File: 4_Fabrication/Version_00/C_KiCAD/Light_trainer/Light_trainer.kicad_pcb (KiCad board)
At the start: 2 copper layers, 70 parts, among them J1 USB_B_Micro, J2 Conn_01x02_Batterie, Q1 DMG3414U, Q2 S8050, Q3 S8050, SW1 SW_Push, SW2 SW_Push, SW3 SW_Push, SW4 SW_Push, SW5 SW_Push, SW6 SW_DIP_x04, SW7 SW_Push, U1 MCP73831-2-OT, U2 ESP32-WROOM-32, U3 LTC3525-5, U4 AP2112K-3.3, U5 CP2104

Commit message: modif kicad
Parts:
- removed Q1: DMG3414U, Package_TO_SOT_SMD:SOT-23
- removed R7: 100k, Resistor_SMD:R_0805_2012Metric
- added J3: Conn_01x09_Female, Connector_PinHeader_1.00mm:PinHeader_1x09_P1.00mm_Vertical, B.Cu at (199.4, 96.5)
- added J4: Conn_01x09_Female, Connector_PinHeader_1.00mm:PinHeader_1x09_P1.00mm_Vertical, F.Cu at (223.5, 96.5)
- added L1: 10uH, Inductor_SMD:L_Wuerth_WE_PMI, F.Cu at (170.2, 111.8)
- added S1: SW_DP3T, Button_Switch_THT:SW_DP3T, F.Cu at (259.1, 102.9)
- C14, C15, R12, R9: moved to B.Cu
- C9: value 10uF -> 1uF
- moved D16 108.1 mm to (172.7, 100.3)
- moved C15 106.4 mm to (240.0, 100.3), turned to 270 degrees
- moved C14 100.8 mm to (236.2, 100.3)
- moved D12 100.0 mm to (227.3, 100.3), turned to 90 degrees
- moved D9 99.9 mm to (238.8, 100.3), turned to 90 degrees
- moved D11 99.7 mm to (231.1, 100.3), turned to 90 degrees
- moved D10 99.6 mm to (234.9, 100.3), turned to 90 degrees
- moved R12 93.4 mm to (232.4, 100.3), turned to 270 degrees
- moved R9 91.0 mm to (228.6, 100.3), turned to 270 degrees
- moved D15 88.3 mm to (148.6, 76.2)
- moved R11 83.3 mm to (194.3, 115.6), turned to 0 degrees
- moved D6 80.9 mm to (207.0, 100.3)
- moved D5 80.8 mm to (196.8, 76.2), turned to 0 degrees
- moved R14 80.1 mm to (154.7, 85.9)
- moved R13 80.1 mm to (157.2, 85.9)
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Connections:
- D4 pad 2: VBUS -> batt_on
- R9 pad 1: (no net) -> Net-(R9-Pad1)
- U2 pad 23: (no net) -> info_batt
- U3 pad 6: (no net) -> Net-(L1-Pad1)

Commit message: modif kicad
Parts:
- added J5: Conn_01x02_Batterie, Connector_Wire:SolderWire-0.1sqmm_1x02_P3.6mm_D0.4mm_OD1mm, F.Cu at (181.6, 124.5)
- moved TP3 74.0 mm to (186.7, 77.5)
- moved TP1 71.1 mm to (186.7, 82.5), turned to 0 degrees
- moved TP2 68.6 mm to (186.7, 87.6), turned to 90 degrees
- moved TP5 46.7 mm to (166.4, 100.3)
- moved J2 26.5 mm to (148.6, 106.7)
- moved R16 7.89 mm to (157.5, 86.4)
- moved R13 7.38 mm to (149.9, 86.4)
- moved R15 2.84 mm to (154.9, 86.4)
- moved R14 2.34 mm to (152.4, 86.4)
- moved C12 1.27 mm to (176.5, 111.8)
- moved TP4 0.57 mm to (186.7, 72.4)
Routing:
- net GND: track 0.00 -> 412.6 mm, vias 0 -> 9
- net +3V3: track 0.00 -> 218.3 mm, vias 0 -> 8
- net +5V: track 0.00 -> 209.6 mm, vias 0 -> 6
- net batt_on: track 0.00 -> 108.4 mm, vias 0 -> 1
- net switch: track 0.00 -> 101.7 mm, vias 0 -> 1
- net +BATT: track 0.00 -> 94.3 mm, vias 0 -> 1
- net EN: track 0.00 -> 69.8 mm, vias 0 -> 2
- net LED_B_3: track 0.00 -> 64.1 mm, vias 0 -> 2
- net VBUS: track 0.00 -> 57.1 mm, vias 0 -> 2
- net D+: track 0.00 -> 45.2 mm, vias 0 -> 2
- net Net-(D15-Pad4): track 0.00 -> 41.9 mm, vias 0 -> 2
- net Net-(D14-Pad4): track 0.00 -> 40.8 mm, vias 0 -> 2
- net stat: track 0.00 -> 39.8 mm, vias 0 -> 2
- net S1: track 0.00 -> 38.7 mm, vias 0 -> 2
- net D-: track 0.00 -> 37.9 mm, vias 0 -> 3
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
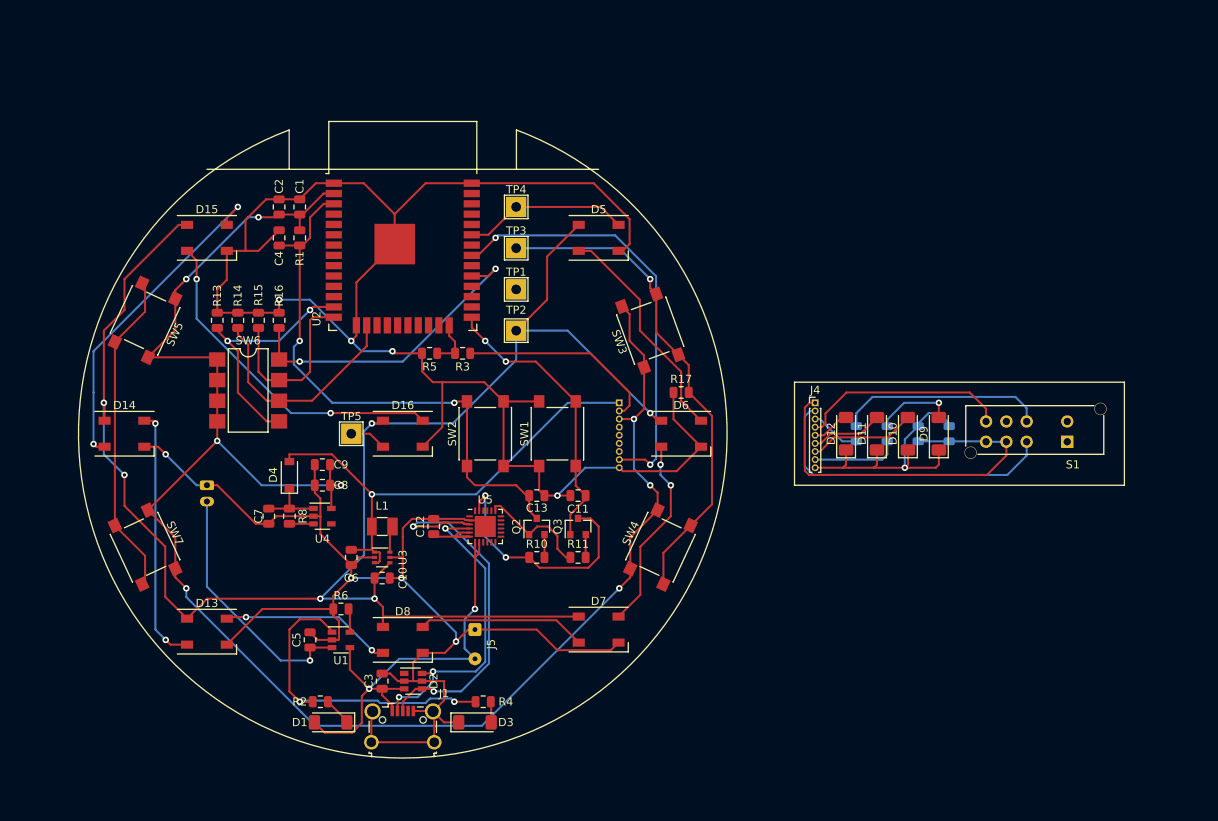
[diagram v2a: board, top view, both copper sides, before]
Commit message: add code
I maybe want to work with pi pico and NRF24l01.
But I have to abandoned my idea of the site web.
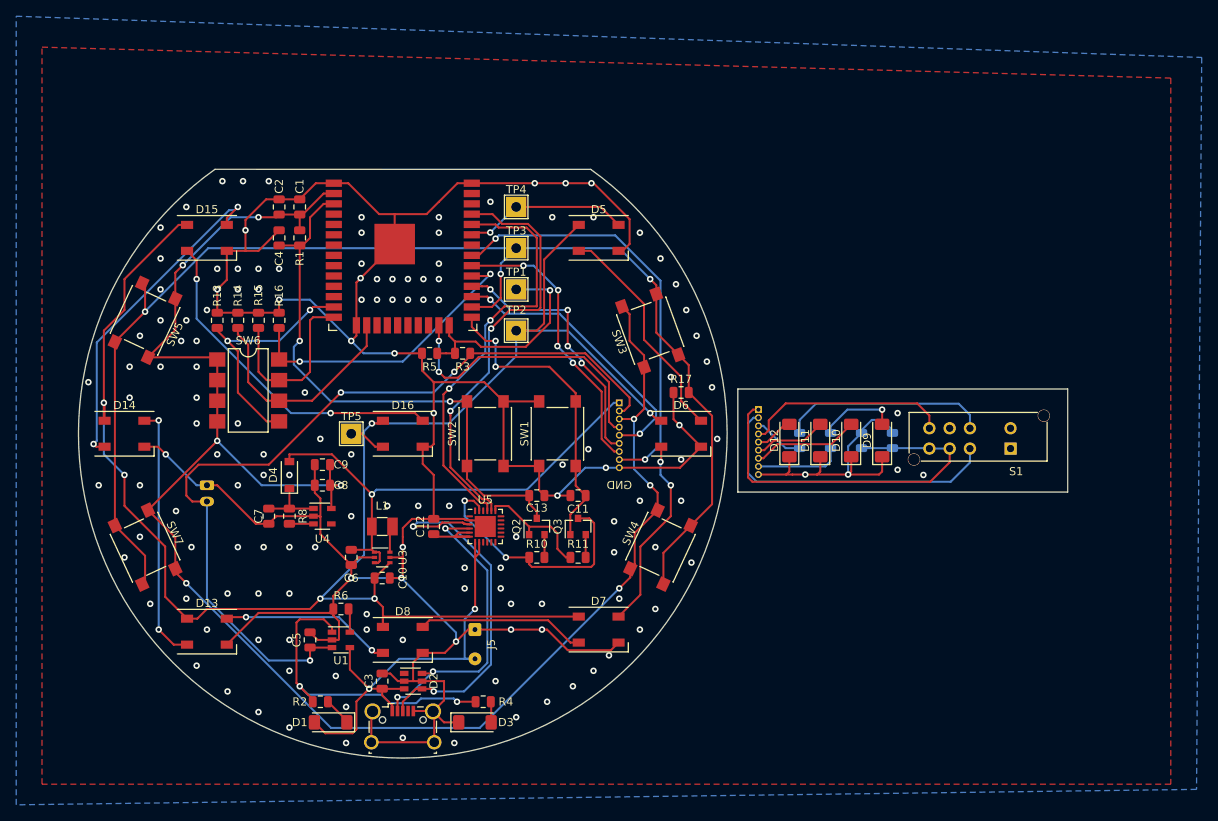
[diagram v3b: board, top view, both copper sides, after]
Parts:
- J4: moved to B.Cu
- moved C15 7.04 mm to (233.0, 101.2)
- moved D12 7.04 mm to (220.3, 101.2)
- moved J4 7.04 mm to (216.5, 97.4), turned to 180 degrees
- moved C14 7.04 mm to (229.2, 101.2)
- moved D10 7.04 mm to (228.0, 101.2)
- moved D11 7.04 mm to (224.2, 101.2)
- moved D9 7.04 mm to (231.8, 101.2)
- moved R12 7.04 mm to (225.4, 101.2)
- moved R9 7.04 mm to (221.6, 101.2)
- moved S1 7.04 mm to (252.1, 103.7)
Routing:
- net switch: track 101.7 -> 161.7 mm, vias 1 -> 3
- net RXD: track 0.00 -> 52.5 mm, vias 0 -> 2
- net TXD: track 0.00 -> 52.0 mm, vias 0 -> 2
- net +BATT: track 94.3 -> 141.3 mm, vias 1 -> 3
- net LED_B_2: track 13.2 -> 48.5 mm, vias 0 -> 4
- net info_batt: track 25.9 -> 61.3 mm, vias 0 -> 2
- net LED_B_0: track 4.72 -> 39.6 mm, vias 0 -> 2
- net LED_B_1: track 8.94 -> 41.6 mm, vias 0 -> 4
- net Net-(R3-Pad2): track 5.93 -> 28.1 mm, vias 0 -> 1
- net GND: track 412.6 -> 421.8 mm, vias 9 -> 148
- net IO0: track 35.5 -> 38.0 mm
- net S1: track 38.7 -> 36.9 mm
- net +5V: track 209.6 -> 210.8 mm
- net VBUS: track 57.1 -> 58.0 mm
- net DTR: track 30.1 -> 31.0 mm
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- added copper zone on B.Cu, net GND
- added copper zone on F.Cu, net GND
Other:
- board outline added: 121.9 x 72.5 mm
- board text added: "GND"
- board text added: "Light Trainer V0 Copyright 2020/2021 Robin Forestier"

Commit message: add datasheet
Restart the project
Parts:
- removed C14, C5, C7, C8: 10uF, Capacitor_SMD:C_0805_2012Metric
- removed C15: 0,1uF, Capacitor_SMD:C_0805_2012Metric
- removed C9: 1uF, Capacitor_SMD:C_0805_2012Metric
- removed D1, D9: LED_R, LED_SMD:LED_1806_4516Metric
- removed D10, D11, D12, D3: LED_G, LED_SMD:LED_1806_4516Metric
- removed D4: MBR0540, Diode_SMD:D_SOD-123
- removed J2: Conn_01x02_Batterie, Connector_JST:JST_PH_B2B-PH-K_1x02_P2.00mm_Vertical
- removed J3, J4: Conn_01x09_Female, Connector_PinHeader_1.00mm:PinHeader_1x09_P1.00mm_Vertical
- removed J5: Conn_01x02_Batterie, Connector_Wire:SolderWire-0.1sqmm_1x02_P3.6mm_D0.4mm_OD1mm
- removed L1: 10uH, Inductor_SMD:L_Wuerth_WE_PMI
- removed R12: 68R, Resistor_SMD:R_0805_2012Metric
- removed R2: 150, Resistor_SMD:R_0805_2012Metric
- removed R4: 100, Resistor_SMD:R_0805_2012Metric
- removed R6: 2K, Resistor_SMD:R_0805_2012Metric
- removed R8: 10k, Resistor_SMD:R_0805_2012Metric
- removed R9: 10K, Resistor_SMD:R_0805_2012Metric
- removed S1: SW_DP3T, Button_Switch_THT:SW_DP3T
- removed U4: AP2112K-3.3, Package_TO_SOT_SMD:SOT-23-5
- U1: value MCP73831-2-OT -> ESP32-DevKitC-32D; footprint Package_TO_SOT_SMD:SOT-23-5 -> Work_Forestier:ESP32-DevKitC-32D
- moved J1 144.8 mm to (45.1, 68.0)
- moved SW4 138.4 mm to (85.7, 43.3), turned to 0 degrees
- moved SW3 132.8 mm to (74.4, 55.1), turned to 0 degrees
- moved D6 132.5 mm to (84.2, 50.6)
- moved SW2 130.5 mm to (56.5, 68.0), turned to 0 degrees
- moved D7 127.2 mm to (106.6, 34.9)
- moved SW1 124.4 mm to (85.7, 35.5), turned to 0 degrees
- moved D8 121.4 mm to (66.3, 67.4)
- moved U2 121.2 mm to (54.1, 53.1)
- moved C3 121.0 mm to (64.3, 72.2), turned to 0 degrees
- moved R17 120.2 mm to (90.1, 67.5)
- moved C11 116.2 mm to (85.7, 66.6), turned to 0 degrees
- moved D2 115.0 mm to (81.3, 62.8)
- moved Q3 113.7 mm to (95.2, 56.1), turned to 0 degrees
- moved Q2 111.0 mm to (90.6, 60.7), turned to 0 degrees
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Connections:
- D2 pad 1: (no net) -> Net-(D2-Pad1)
- J1 pad 4: (no net) -> Net-(J1-Pad4)
- U2 pad 10: (no net) -> Net-(U2-Pad10)
- U2 pad 11: (no net) -> Net-(U2-Pad11)
- U2 pad 12: (no net) -> Net-(U2-Pad12)
- U2 pad 17: (no net) -> Net-(U2-Pad17)
- U2 pad 18: (no net) -> Net-(U2-Pad18)
- U2 pad 19: (no net) -> Net-(U2-Pad19)
- U2 pad 20: (no net) -> Net-(U2-Pad20)
- U2 pad 21: (no net) -> Net-(U2-Pad21)
- U2 pad 22: (no net) -> Net-(U2-Pad22)
- U2 pad 32: (no net) -> Net-(U2-Pad32)
- U2 pad 36: (no net) -> Net-(U2-Pad36)
- U2 pad 37: (no net) -> Net-(U2-Pad37)
- U2 pad 4: (no net) -> Net-(U2-Pad4)
- U2 pad 5: (no net) -> Net-(U2-Pad5)
- U2 pad 6: (no net) -> Net-(U2-Pad6)
- U2 pad 7: (no net) -> Net-(U2-Pad7)
- U2 pad 8: (no net) -> Net-(U2-Pad8)
- U2 pad 9: (no net) -> Net-(U2-Pad9)
- U5 pad 1: (no net) -> Net-(U5-Pad1)
- U5 pad 10: (no net) -> Net-(U5-Pad10)
- U5 pad 11: (no net) -> Net-(U5-Pad11)
- U5 pad 12: (no net) -> Net-(U5-Pad12)
- U5 pad 13: (no net) -> Net-(U5-Pad13)
- U5 pad 14: (no net) -> Net-(U5-Pad14)
- U5 pad 15: (no net) -> Net-(U5-Pad15)
- U5 pad 16: (no net) -> Net-(U5-Pad16)
- U5 pad 17: (no net) -> Net-(U5-Pad17)
- U5 pad 18: (no net) -> Net-(U5-Pad18)
- U5 pad 22: (no net) -> Net-(U5-Pad22)
- U5 pad 24: (no net) -> Net-(U5-Pad24)
- U5 pad 9: (no net) -> Net-(U5-Pad9)
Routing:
- net GND: track 421.8 -> 0.00 mm, vias 148 -> 0
- net +3V3: track 218.7 -> 0.00 mm, vias 8 -> 0
- net +5V: track 210.8 -> 0.00 mm, vias 6 -> 0
- net switch: track 161.7 -> 0.00 mm, vias 3 -> 0
- net +BATT: track 141.3 -> 0.00 mm, vias 3 -> 0
- net batt_on: track 108.4 -> 0.00 mm, vias 1 -> 0
- net EN: track 69.8 -> 0.00 mm, vias 2 -> 0
- net LED_B_3: track 63.3 -> 0.00 mm, vias 2 -> 0
- net info_batt: track 61.3 -> 0.00 mm, vias 2 -> 0
- net VBUS: track 58.0 -> 0.00 mm, vias 2 -> 0
- net RXD: track 52.5 -> 0.00 mm, vias 2 -> 0
- net TXD: track 52.0 -> 0.00 mm, vias 2 -> 0
- net LED_B_2: track 48.5 -> 0.00 mm, vias 4 -> 0
- net D+: track 45.6 -> 0.00 mm, vias 2 -> 0
- net Net-(D15-Pad4): track 41.9 -> 0.00 mm, vias 2 -> 0
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- removed copper zone on B.Cu, net GND
- removed copper zone on F.Cu, net GND
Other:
- board outline removed
- board text removed: "GND"
- board text removed: "Light Trainer V0 Copyright 2020/2021 Robin Forestier"
